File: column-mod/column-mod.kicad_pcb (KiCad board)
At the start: 2 copper layers, 18.9 x 15.2 mm, 12 parts, among them J1 Conn_01x01, J10 Conn_01x01, J11 Conn_01x05_Female, J2 Conn_01x01, J3 Conn_01x01, J4 Conn_01x01, J5 Conn_01x01, J6 Conn_01x01, J7 Conn_01x01, J8 Conn_01x01, J9 Conn_01x01

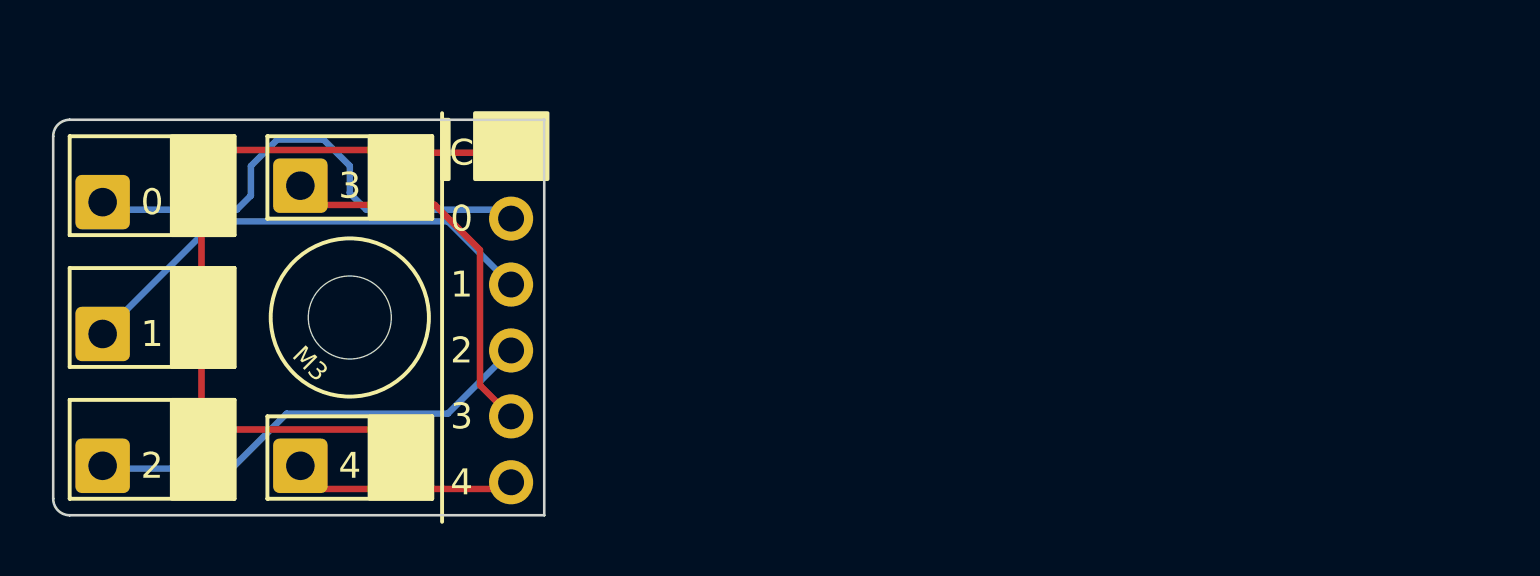
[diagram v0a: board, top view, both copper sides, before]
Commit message: Rework the column module -- add JST connector & diodes
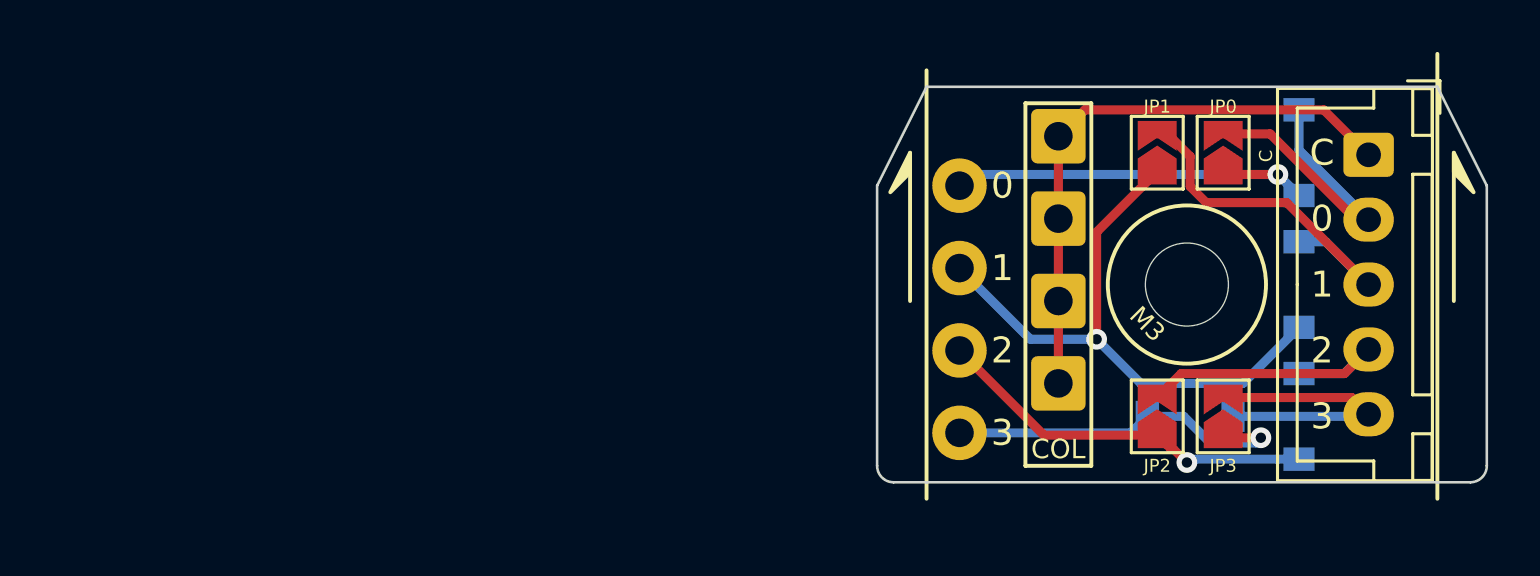
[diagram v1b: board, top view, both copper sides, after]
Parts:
- removed J10, J5: Conn_01x01, Connector_Wire:SolderWire-0.5sqmm_1x01_D0.9mm_OD2.1mm
- added D0: D, Library:D_SOD-123, B.Cu at (168.7, 66.0)
- added D1: D, Library:D_SOD-123, B.Cu at (168.7, 71.1)
- added D2: D, Library:D_SOD-123, B.Cu at (168.7, 76.2)
- added D3: D, Library:D_SOD-123, B.Cu at (164.5, 76.2)
- added JP0: Jumper_2_Open, Library:SolderJumper-Open, F.Cu at (165.7, 66.0)
- added JP1: Jumper_2_Open, Library:SolderJumper-Open, F.Cu at (163.2, 66.0)
- added JP2: Jumper_2_Open, Library:SolderJumper-Open, F.Cu at (163.2, 76.2)
- added JP3: Jumper_2_Open, Library:SolderJumper-Open, F.Cu at (165.7, 76.2)
- J_A1: renamed from J11; value Conn_01x05_Female -> Conn_01x05; footprint Connector_PinSocket_2.54mm:PinSocket_1x06_P2.54mm_Vertical -> Connector_JST:JST_XH_B5B-XH-A_1x05_P2.50mm_Vertical
- moved J2 33.3 mm to (155.6, 73.7), turned to 180 degrees
- moved J_C1 33.2 mm to (159.4, 68.6)
- moved J1 33.1 mm to (155.6, 70.5), turned to 180 degrees
- moved J_C2 33.1 mm to (159.4, 74.9)
- moved J_A1 33.0 mm to (171.3, 66.1), turned to -90 degrees
- moved J_C0 33.0 mm to (159.4, 65.4)
- moved J0 33.0 mm to (155.6, 67.3), turned to 180 degrees
- moved H1 32.3 mm to (164.3, 71.1)
- moved J3 27.1 mm to (155.6, 76.8), turned to 180 degrees
- moved J_C3 25.9 mm to (159.4, 71.8)
- renumbered J6 to J0, J7 to J1, J8 to J2, J9 to J3, J1 to J_C0, J2 to J_C1, J3 to J_C2, J4 to J_C3
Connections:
- J0 pad 1: Net-(J11-Pad2) -> Net-(D0-Pad2)
- J1 pad 1: Net-(J11-Pad3) -> Net-(D1-Pad2)
- J2 pad 1: Net-(J11-Pad4) -> Net-(D2-Pad2)
- J3 pad 1: Net-(J9-Pad1) -> Net-(D3-Pad2)
- J_A1 pad 2: Net-(J11-Pad2) -> /r0
- J_A1 pad 3: Net-(J11-Pad3) -> /r1
- J_A1 pad 4: Net-(J11-Pad4) -> /r2
- J_A1 pad 5: Net-(J9-Pad1) -> /r3
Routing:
- net Net-(D1-Pad2): track 0.00 -> 23.2 mm, vias 0 -> 1
- net Net-(J11-Pad2): track 21.4 -> 0.00 mm
- net Net-(J11-Pad3): track 18.5 -> 0.00 mm
- net Net-(J11-Pad4): track 17.7 -> 0.00 mm
- net Net-(D2-Pad2): track 0.00 -> 15.0 mm, vias 0 -> 1
- net Net-(D0-Pad2): track 0.00 -> 15.0 mm, vias 0 -> 1
- net Net-(J9-Pad1): track 14.9 -> 0.00 mm
- net /r1: track 0.00 -> 14.6 mm
- net Net-(D3-Pad2): track 0.00 -> 13.7 mm, vias 0 -> 1
- net /r2: track 0.00 -> 12.0 mm
- net /r0: track 0.00 -> 11.8 mm
- net /r3: track 0.00 -> 11.0 mm
- net Net-(J11-Pad6): track 8.23 -> 0.00 mm
- net /c: track 28.0 -> 22.6 mm
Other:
- board size 18.9 x 15.2 mm -> 23.5 x 15.2 mm
- board text added: "C"
- board text added: "COL"
- board text added: "COLUMN MODULE v1"
- board text added: "github.com/encukou/squeezebar"
- board text removed: "4"
